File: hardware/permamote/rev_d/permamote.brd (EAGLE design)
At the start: 27 x 60 mm, 126 parts, among them J1 TC2030-JLINK-NL, J5 MICRO_USB_B_HIROSE_ZX62R-B-5P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, Q1 PMDXB950UPEL, Q10 PMDXB950UPEL, Q2 PMDXB950UPEL, Q3 PMDXB950UPEL, Q4 PMDXB950UPEL, Q5 PMDXB950UPEL, Q6 PMDXB950UPEL, Q7 PMDXB950UPEL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

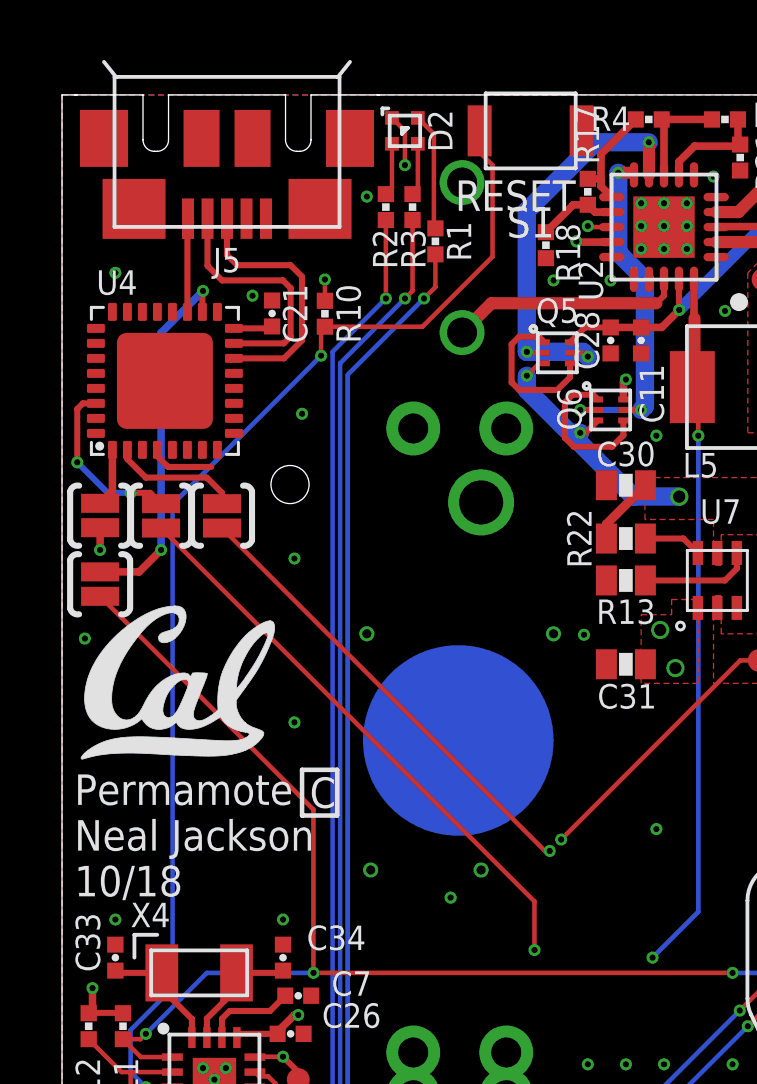
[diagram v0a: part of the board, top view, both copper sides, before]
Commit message: Fix exti in rev d
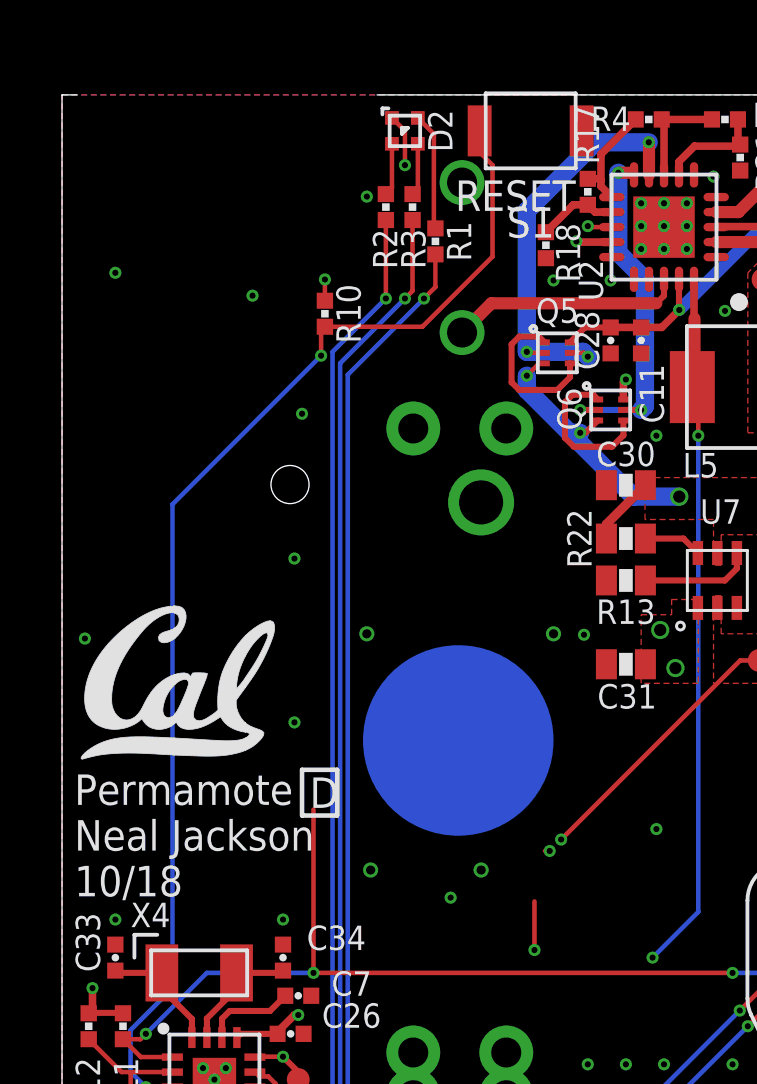
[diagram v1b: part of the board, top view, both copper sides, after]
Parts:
- removed C21: 0.1uF, passives:0402_CAP
- removed J5: MICRO_USB_B_HIROSE_ZX62R-B-5P(30), connector:MICRO_USB_B_HIROSE_ZX62R-B-5P(30)
- removed SJ2, SJ3, SJ4, SJ5: SOLDERJUMPERNC2, SparkFun-Passives:SJ_2S-NOTRACE
- removed U4: FT232RQ, ftdichip:QFN32
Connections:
- removed net !FTDI_RESET: SJ3.2, U4.18
- removed net D+: J5.3, U4.14
- removed net D-: J5.2, U4.15
- removed net FTDI_VCCIO: SJ2.2, U4.1
- removed net N$13: C21.1, U4.16
- removed net RXD: SJ4.1, U4.2
- removed net TXD: SJ5.1, U4.30
- removed net USB_5V: J5.1, U4.19
- net !RST: no longer SJ3.1
- net DBG_RX: no longer SJ5.2
- net DBG_TX: no longer SJ4.2
- net GND: now also U1.10; no longer C21.2, J5.5, U4.17, U4.20, U4.24, U4.26, U4.4
- net VCC: no longer SJ2.1
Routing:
- net DBG_RX: track 41.0 -> 23.4 mm
- net DBG_TX: track 37.5 -> 22.2 mm
- net !FTDI_RESET: track 12.3 -> 0.00 mm, vias 2 -> 0
- net !RST: track 65.5 -> 55.4 mm
- net D+: track 8.66 -> 0.00 mm
- net D-: track 8.25 -> 0.00 mm
- net TXD: track 5.84 -> 0.00 mm, vias 2 -> 0
- net RXD: track 4.29 -> 0.00 mm
- net USB_5V: track 3.20 -> 0.00 mm
- net GND: track 24.3 -> 22.2 mm
- net FTDI_VCCIO: track 1.95 -> 0.00 mm
- net N$13: track 1.30 -> 0.00 mm
- net VCC: track 67.5 -> 66.8 mm, vias 29 -> 28

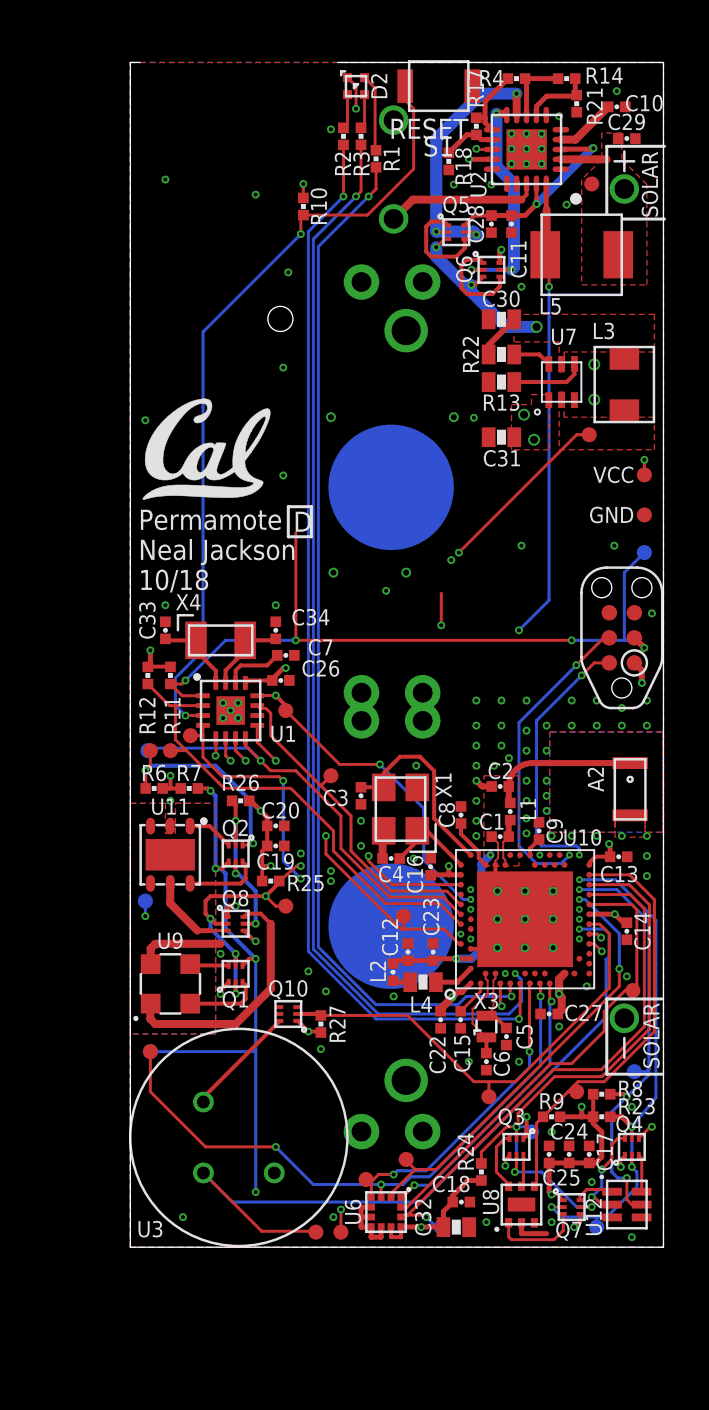
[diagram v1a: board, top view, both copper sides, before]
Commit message: switch to larger coin cell, new light sensor
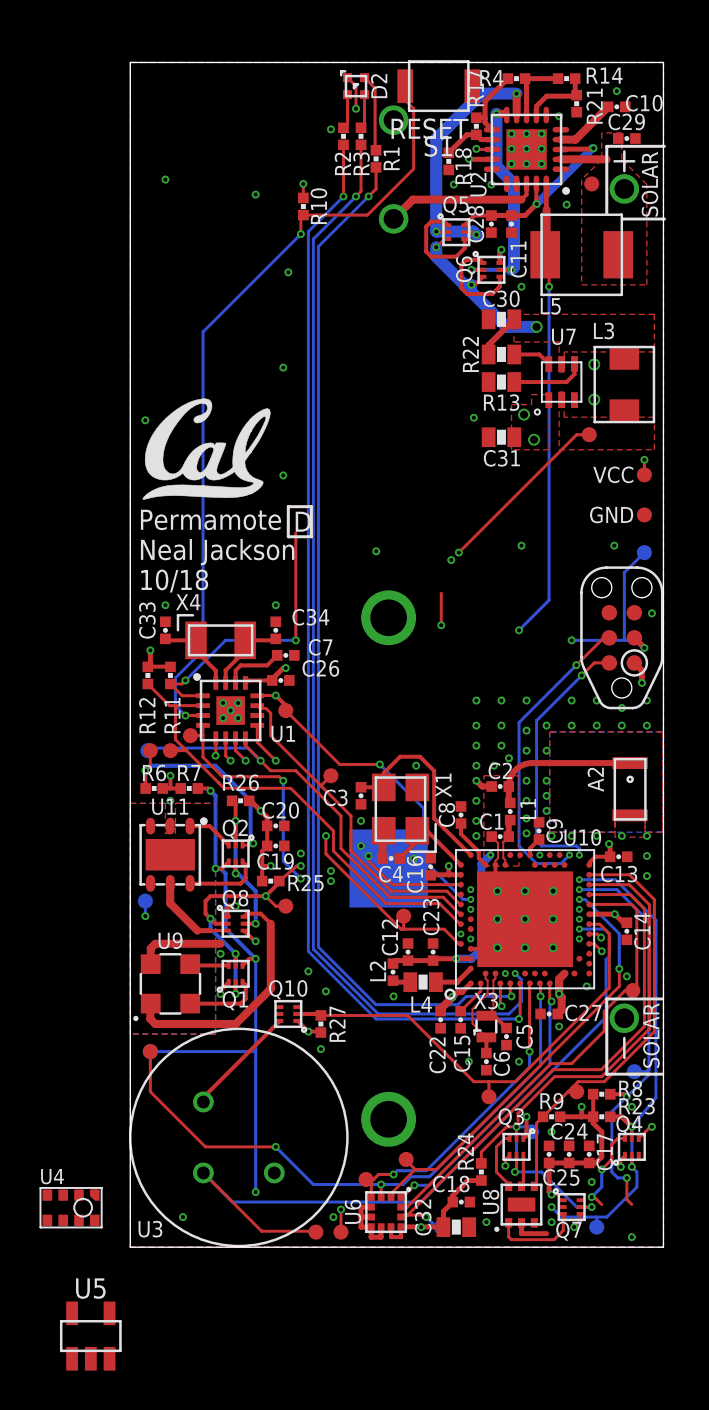
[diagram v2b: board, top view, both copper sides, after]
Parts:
- removed BT2, BT3: BAT-HLD-002-THM, batteries:BAT-HLD-002-THM
- removed BT4: BAT_PACKCR123A, batteries:BH123A
- removed U12: TCS34725, chips:FN-6
- added BAT1: 2477THMCOINCELLCLIP, batteries:2477THMCOINCLIP
- added U4: AS7341, chips:OLGA-8
- added U5: MCP1810T-18I/TT, chips:SOT-23-5
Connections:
- removed net N$54: Q4.3, U12.6
- new net N$13: Q4.3, U4.8
- net !CLR_EN: now also U5.2; no longer Q7.2
- net !CLR_INT: now also U4.7; no longer U12.5
- net GND: now also BAT1.GND, U4.3, U4.5, U5.5; no longer BT2.GND, BT3.GND, BT4.-, U12.3
- net N$31: now also U4.1, U5.3; no longer Q7.6, U12.1
- net N$55: now also U4.2; no longer U12.2
- net VBAT: now also BAT1.1, BAT1.2; no longer BT2.POS1, BT2.POS2, BT2.POS3, BT2.POS4, BT3.POS1, BT3.POS2, BT3.POS3, BT3.POS4, BT4.+
- net VCC: now also U5.1; no longer Q7.1
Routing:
- net !RST: track 55.4 -> 41.5 mm
- net VCC: track 66.8 -> 53.7 mm, vias 28 -> 24
- net SCL: track 56.3 -> 47.1 mm
- net VBAT: track 23.9 -> 21.7 mm
- net N$31: track 2.01 -> 0.00 mm
- net N$54: track 1.91 -> 0.00 mm
- net !CLR_EN: track 27.5 -> 26.9 mm
- net N$55: track 5.06 -> 4.54 mm
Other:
- outline, holes or cut-outs redrawn
- board text removed: "CR123A PACK +"
